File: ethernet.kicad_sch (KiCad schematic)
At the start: 0 parts

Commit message: Finishing up the schematic for the gigabit ethernet
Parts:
- added C33, C34, C35, C36, C37, C40, C41: 100nF/50v, A_HDJ_Library:C_0402_1005Metric, symbol Device:C_Small
- added C38, C39, C42, C43, C44, C45: 10uF/50v, A_HDJ_Library:C_0402_1005Metric, symbol Device:C_Small
- added C46, C47: 12pF/50V, symbol Device:C
- added C88: 100nF/50V, A_HDJ_Library:C_0402_1005Metric, symbol Device:C
- added J6: RJ45_RB1-125B8G1A, A_HDJ_Library:RJ45_UDE_RB1-125B8G1A, symbol Connector:RJ45_RB1-125B8G1A
- added R20: 10\K/1%, A_HDJ_Library:R_0603_1608Metric, symbol Device:R
- added R21: 10k/1%, A_HDJ_Library:R_0603_1608Metric, symbol Device:R
- added R22: 2.49K/1%, A_HDJ_Library:R_0603_1608Metric, symbol Device:R
- added R23: 1M/1%, A_HDJ_Library:R_0402_1005Metric, symbol Device:R
- added R24, R25: 470R/1%, A_HDJ_Library:R_0402_1005Metric, symbol Device:R
- added U6: RTL8111H-CG-RH, A_HDJ_Library:QFN-32-1EP_4x4mm_P0.4mm_EP2.65x2.65mm, symbol A_HDJ_Library:RTL8111H-CG-RH
- added U7, U79: D3V3XA4B10LP, Package_DFN_QFN:Diodes_UDFN-10_1x2.5mm_P0.5mm, symbol Power_Protection:D3V3XA4B10LP
- added Y1: 25MHz, symbol Device:Crystal_GND24
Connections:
- new net: C46.1, R23.2, U6.29 (CKXTAL2), Y1.3
- new net: R22.1, U6.31 (RSET)
- new net: R20.2, U6.20 (ISOLATEB)
- new net: R21.2, U6.21 (LANWAKEB)
- new net: J6.L2, U6.25 (LED2)
- new net: J6.L4, U6.26 (LED1)
- new net: C47.1, R23.1, U6.28 (CKXTAL1), Y1.1
- new net: J6.L1, R25.1
- new net: J6.L3, R24.1
- new net: C88.2, J6.R1 (CT)
- new net +1V0: C33.1, C34.1, C35.1, C36.1, C40.1, C44.1, U6.22 (DVDD10), U6.24 (REGOUT), U6.3 (AVDD10), U6.30 (AVDD10), U6.8 (AVDD10)
- new net +3.3V: C37.1, C41.1, C45.1, R20.1, R21.1, R24.2, R25.2, U6.11 (AVDD33)
- new net GND: C33.2, C34.2, C35.2, C36.2, C37.2, C40.2, C41.2, C44.2, C45.2, C46.2, C47.2, C88.1, J6.R10 (GND), J6.SH, R22.2, U6.33 (GND), U7.3 (VSS), U7.8 (VSS), U79.3 (VSS), U79.8 (VSS), Y1.4 (G)
- new net GbE_PCIe_CLK+: U6.15 (REFCLK_P)
- new net GbE_PCIe_CLK-: U6.16 (REFCLK_N)
- new net GbE_PCIe_RX+: C43.1
- new net GbE_PCIe_RX-: C39.1
- new net GbE_PCIe_TX+: C42.1
- new net GbE_PCIe_TX-: C38.1
- new net HSI+: C38.2, C39.2, U6.14 (HSIN), U6.18 (HSON)
- new net HSI-: C42.2, C43.2, U6.13 (HSIP), U6.17 (HSOP)
- new net MDI0+: J6.R2 (TD1+), U6.1 (MDIP0), U7.5, U7.6 (NC)
- new net MDI0-: J6.R3 (TD1-), U6.2 (MDIN0), U7.4, U7.7 (NC)
- new net MDI1+: J6.R4 (TD2+), U6.4 (MDIP1), U7.2, U7.9 (NC)
- new net MDI1-: J6.R5 (TD2-), U6.5 (MDIN1), U7.1, U7.10 (NC)
- new net MDI2+: J6.R7 (TD3-), U6.7 (MDIN2), U79.4, U79.7 (NC)
- new net MDI2-: J6.R6 (TD3+), U6.6 (MDIP2), U79.5, U79.6 (NC)
- new net MDI3+: J6.R8 (TD4+), U6.9 (MDIP3), U79.2, U79.9 (NC)
- new net MDI3-: J6.R9 (TD4-), U6.10 (MDIN3), U79.1, U79.10 (NC)
- new net ~{PLT_RST}: U6.19 (PERSTB)
- no-connect marks 0 -> 2

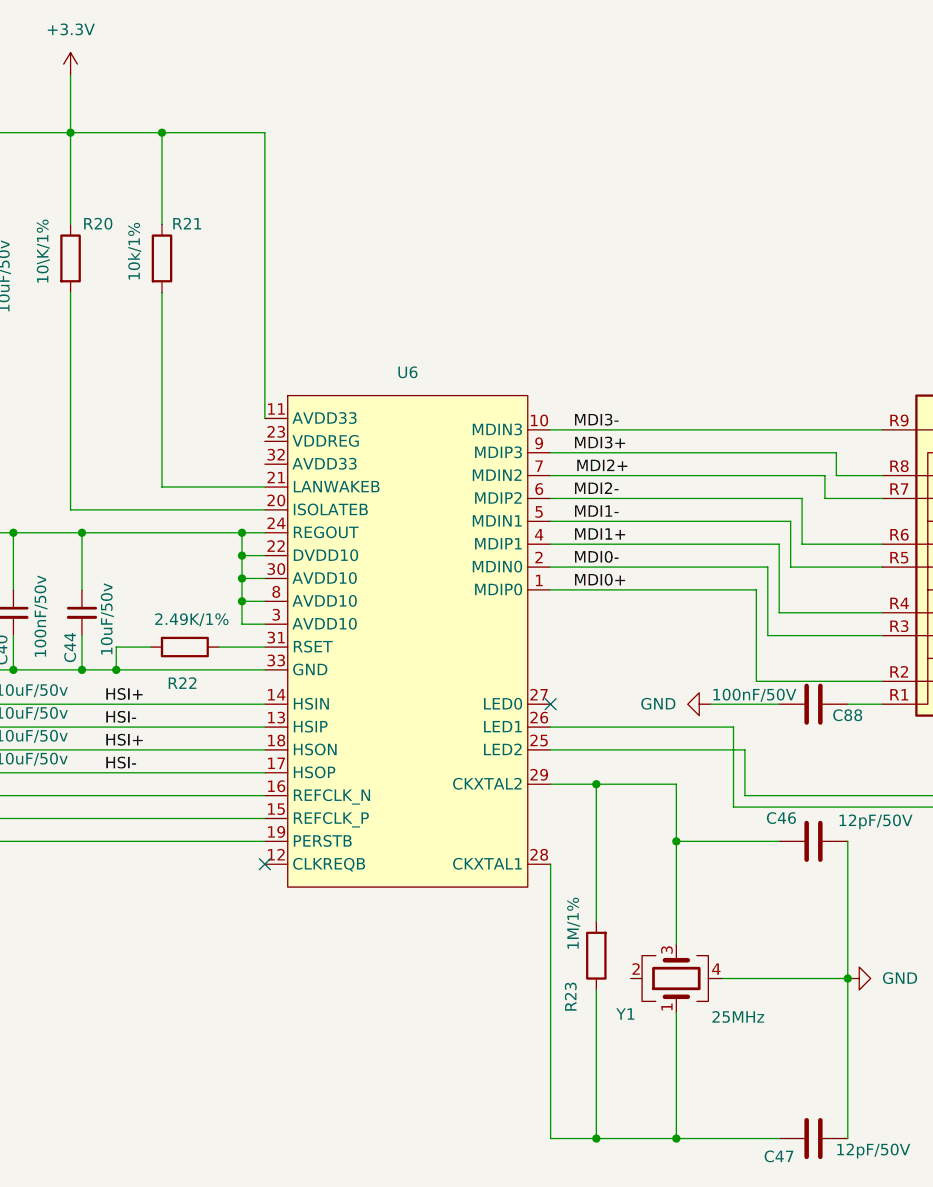
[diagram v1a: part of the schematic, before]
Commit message: Fixed some ERC errors int the gigabit sub schema
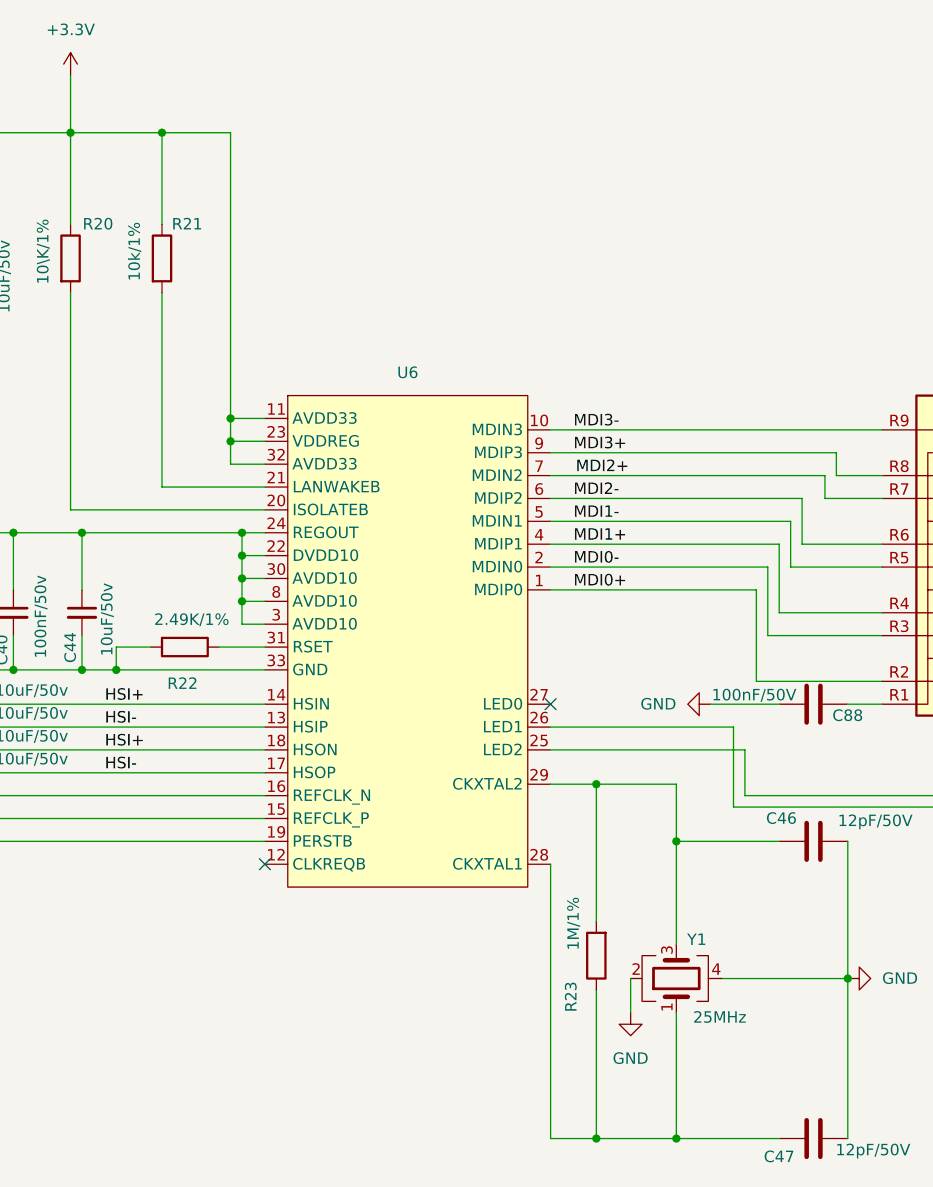
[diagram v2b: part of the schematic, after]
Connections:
- net +3.3V: now also U6.23 (VDDREG), U6.32 (AVDD33)
- net GND: now also Y1.2 (G)
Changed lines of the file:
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@@
 	)
 	(junction
+		(at 90.17 64.77)
+		(diameter 0)
+		(color 0 0 0 0)
+	)
+	(junction
+		(at 90.17 62.23)
+		(diameter 0)
+		(color 0 0 0 0)
+	)
+	(junction
 		(at 130.81 102.87)
 		(diameter 0)
@@
 	(wire
 		(pts
+			(xy 134.62 128.27) (xy 134.62 124.46)
+		)
+		(stroke
+			(width 0)
+			(type default)
+		)
+	)
+	(wire
+		(pts
 			(xy 35.56 90.17) (xy 43.18 90.17)
 		)
@@
 	(wire
 		(pts
+			(xy 90.17 67.31) (xy 90.17 64.77)
+		)
+		(stroke
+			(width 0)
+			(type default)
+		)
+	)
+	(wire
+		(pts
+			(xy 93.98 67.31) (xy 90.17 67.31)
+		)
+		(stroke
+			(width 0)
+			(type default)
+		)
+	)
+	(wire
+		(pts
 			(xy 77.47 90.17) (xy 93.98 90.17)
 		)
@@
 	(wire
 		(pts
-			(xy 82.55 30.48) (xy 93.98 30.48)
+			(xy 82.55 30.48) (xy 90.17 30.48)
 		)
 		(stroke
@@
 	(wire
 		(pts
-			(xy 93.98 62.23) (xy 93.98 30.48)
+			(xy 90.17 62.23) (xy 93.98 62.23)
 		)
 		(stroke
@@
 	(wire
 		(pts
+			(xy 90.17 64.77) (xy 90.17 62.23)
+		)
+		(stroke
+			(width 0)
+			(type default)
+		)
+	)
+	(wire
+		(pts
 			(xy 43.18 86.36) (xy 43.18 90.17)
 		)
@@
 	(wire
 		(pts
+			(xy 90.17 64.77) (xy 93.98 64.77)
+		)
+		(stroke
+			(width 0)
+			(type default)
+		)
+	)
+	(wire
+		(pts
 			(xy 151.13 142.24) (xy 139.7 142.24)
 		)
@@
 	(wire
 		(pts
+			(xy 90.17 62.23) (xy 90.17 30.48)
+		)
+		(stroke
+			(width 0)
+			(type default)
+		)
+	)
+	(wire
+		(pts
 			(xy 205.74 100.33) (xy 215.9 100.33)
 		)
@@
 		(dnp no)
 		(property "Reference" "Y1"
-			(at 134.112 128.4538 90)
+			(at 141.986 120.142 90)
 			(show_name no)
 			(do_not_autoplace no)
@@
 		)
 		(property "Value" "25MHz"
-			(at 146.558 128.778 90)
+			(at 144.526 128.778 90)
 			(show_name no)
 			(do_not_autoplace no)
@@
 					(unit 1)
 				)
+			)
+		)
+	)
+	(symbol
+		(lib_id "power:GND")
+		(at 134.62 128.27 0)
+		(unit 1)
+		(body_style 1)
+		(exclude_from_sim no)
+		(in_bom yes)
+		(on_board yes)
+		(in_pos_files yes)
+		(dnp no)
+		(fields_autoplaced yes)
+		(property "Reference" "#PWR0174"
+			(at 134.62 134.62 0)
+			(hide yes)
+			(show_name no)
+			(do_not_autoplace no)
+			(effects
+				(font
+					(size 1.27 1.27)
+				)
+			)
+		)
+		(property "Value" "GND"
+			(at 134.62 133.35 0)
+			(show_name no)
+			(do_not_autoplace no)
+			(effects
+				(font
+					(size 1.27 1.27)
+				)
+			)
+		)
+		(property "Footprint" ""
+			(at 134.62 128.27 0)
+			(hide yes)
+			(show_name no)
+			(do_not_autoplace no)
+			(effects
+				(font
+					(size 1.27 1.27)
+				)
+			)
+		)
+		(property "Datasheet" ""
+			(at 134.62 128.27 0)
+			(hide yes)
+			(show_name no)
+			(do_not_autoplace no)
+			(effects
+				(font
+					(size 1.27 1.27)
+				)
+			)
+		)
+		(property "Description" "Power symbol creates a global label with name \"GND\" , ground"
+			(at 134.62 128.27 0)
+			(hide yes)
+			(show_name no)
+			(do_not_autoplace no)
+			(effects
+				(font
+					(size 1.27 1.27)
+				)
+			)
+		)
+		(pin "1"
+		)
+		(instances
+			(project "Carrier_Board"
+				(path "/e768274e-12f3-4f83-96f6-abb7638e0bc1/3ad1df68-0a03-497a-a7ee-c67c9856d4e6"
+					(reference "#PWR0174")
+					(unit 1)
+				)
